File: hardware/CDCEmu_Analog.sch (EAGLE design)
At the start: 63 parts, among them J1 Audio In, J2 Audio Out, J3 Mic In, Q1 PCH, Q2 NCH, Q3 NCH, Q4 PCH, Q5 NCH, Q6 NPN, Q7 NPN, Q8 NPN, Q9 NPN, U1 1117, U2 BK8000L, U3 NE5532D

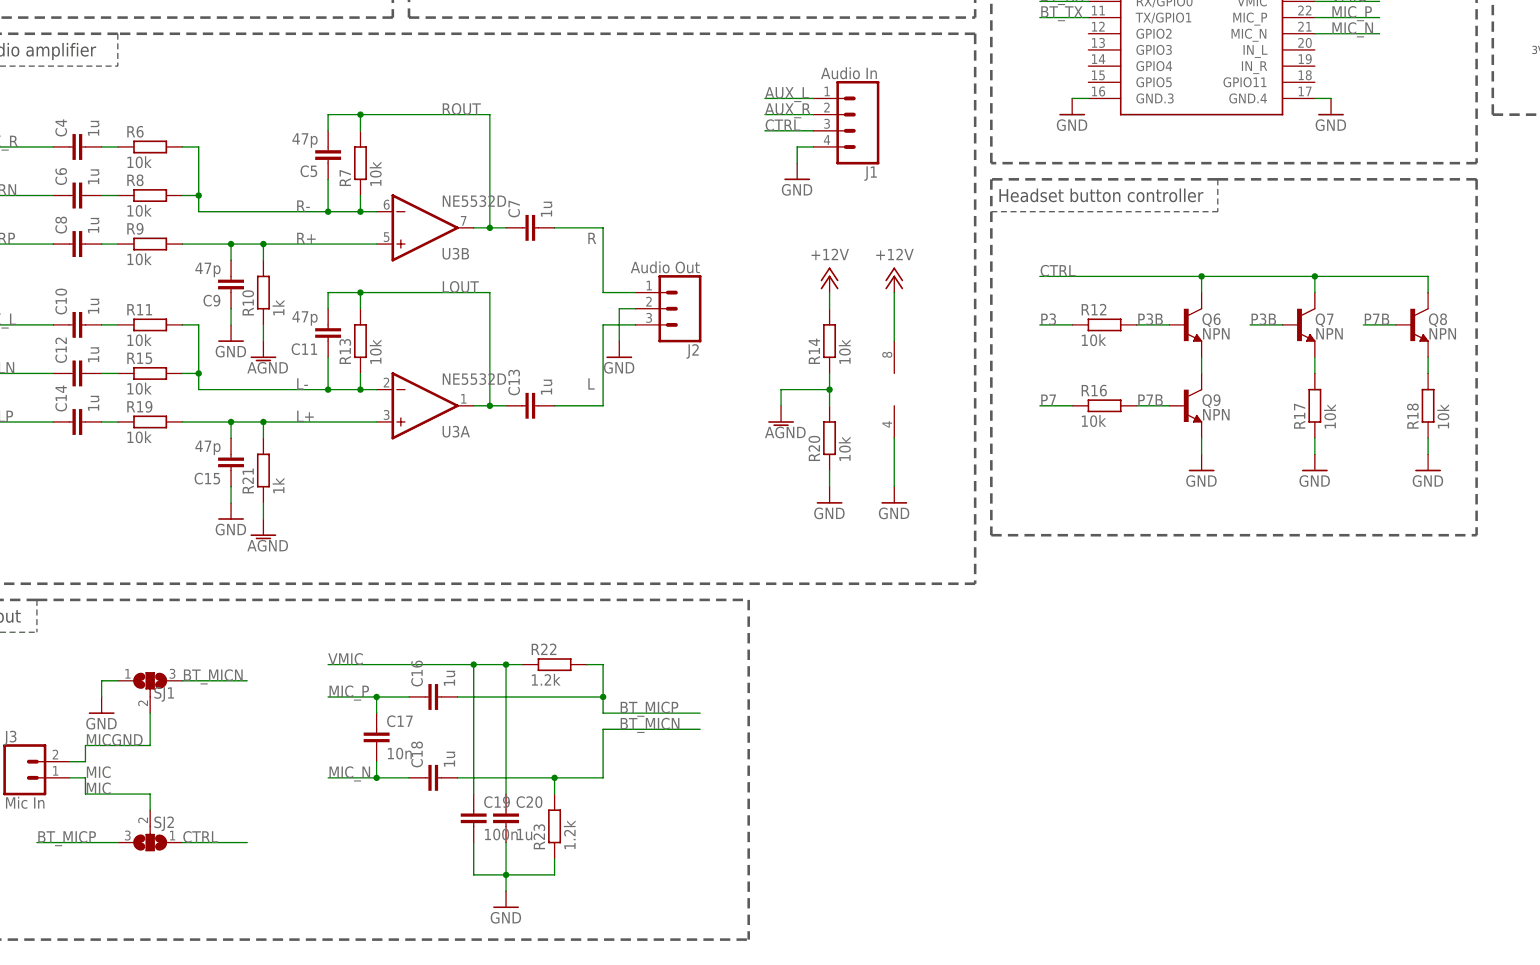
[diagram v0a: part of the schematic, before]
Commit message: [HW] Add audio gain control trimpots
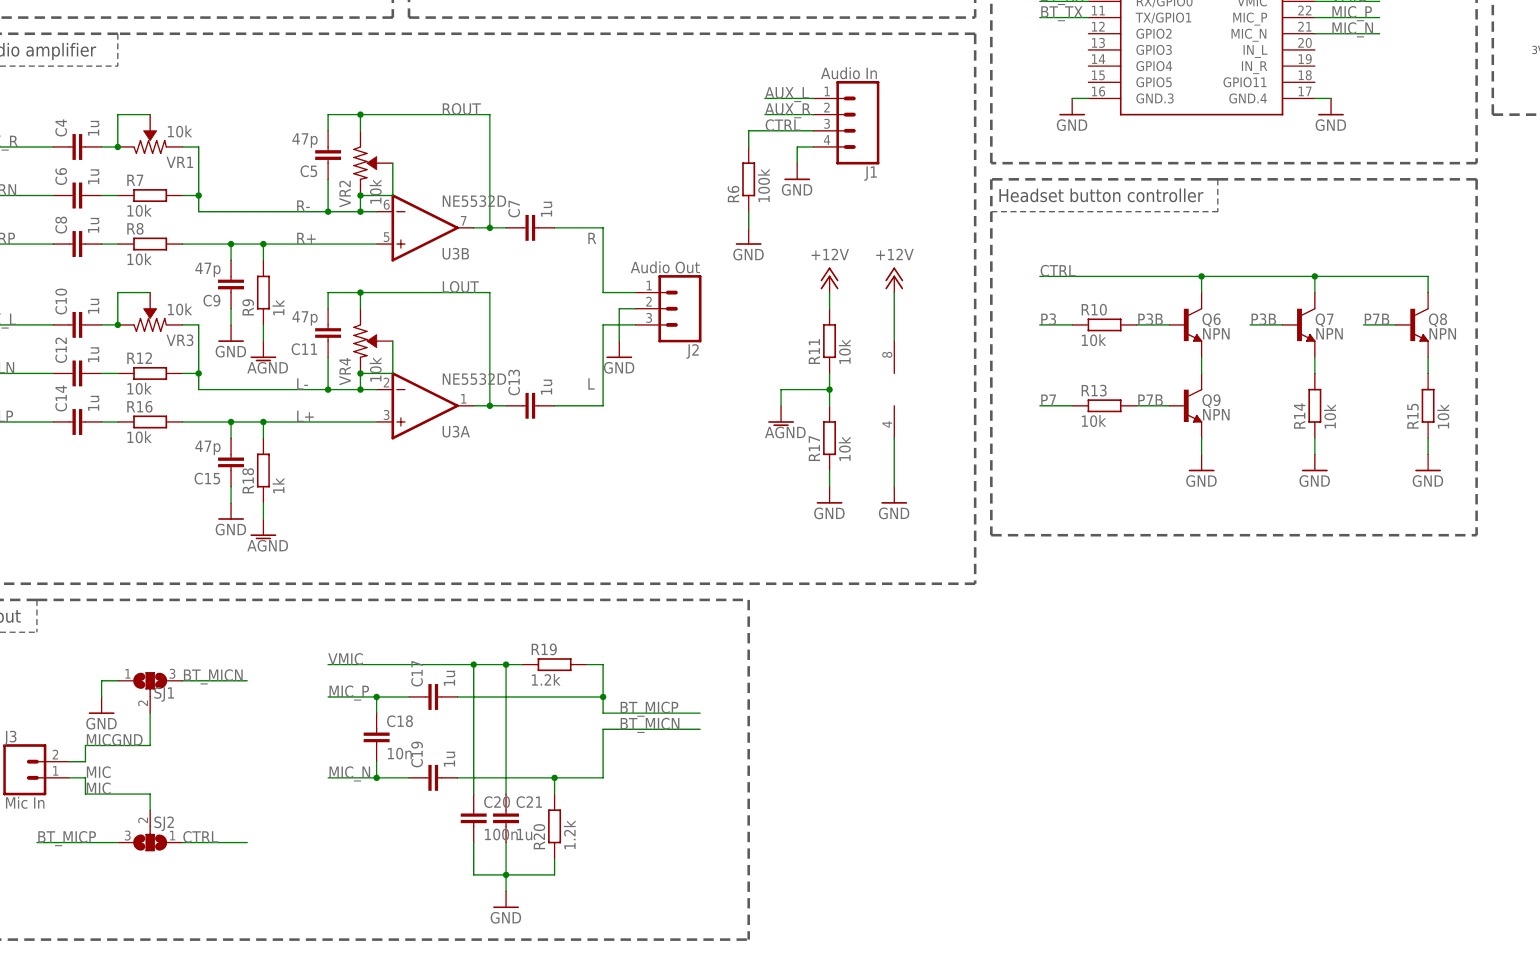
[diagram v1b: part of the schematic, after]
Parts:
- removed C16: 1u, rcl:C-EUC0805
- removed R21: 1k, rcl:R-EU_R0805
- removed R22, R23: 1.2k, rcl:R-EU_R0805
- added C21: 1u, rcl:C-EUC0805
- added VR1, VR2, VR3, VR4: 10k, SparkFun-Resistors:TRIMPOT-SMD-3MM-OPEN-1/10W-25%
- C17: value 10n -> 1u
- C18: value 1u -> 10n
- C19: value 100n -> 1u
- C20: value 1u -> 100n
- R10: value 1k -> 10k
- R18, R9: value 10k -> 1k
- R19, R20: value 10k -> 1.2k
- R6: value 10k -> 100k
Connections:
- net +12V: now also R11.2; no longer R14.2
- net AGND: now also R11.1, R17.2, R18.1, R9.1; no longer R10.1, R14.1, R20.2, R21.1
- net BT_MICN: now also C19.2, R20.2; no longer C18.2, R23.2
- net BT_MICP: now also C17.2, R19.2; no longer C16.2, R22.2
- net CTRL: now also R6.2
- net GND: now also C21.2, R14.1, R15.1, R6.1; no longer C19.2, R18.1, R23.1
- net L+: now also R16.2, R18.2; no longer R19.2, R21.2
- net L-: now also R12.2, VR3.CCW, VR4.CCW, VR4.WIPER; no longer R11.2, R13.1, R15.2
- net L1: now also VR3.CW, VR3.WIPER; no longer R11.1
- net L2: now also R12.1; no longer R15.1
- net L3: now also R16.1; no longer R19.1
- net LOUT: now also VR4.CW; no longer R13.2
- net MIC_N: now also C18.2, C19.1; no longer C17.2, C18.1
- net MIC_P: now also C18.1; no longer C16.1
- net P3: now also R10.1; no longer R12.1
- net P3B: now also R10.2; no longer R12.2
- net P7: now also R13.1; no longer R16.1
- net P7B: now also R13.2; no longer R16.2
- net Q7E: now also R14.2; no longer R17.2
- net Q8E: now also R15.2; no longer R18.2
- net R+: now also R8.2; no longer R10.2
- net R-: now also R7.2, VR1.CCW, VR2.CCW, VR2.WIPER; no longer R6.2, R7.1, R8.2
- net R1: now also VR1.CW, VR1.WIPER; no longer R6.1
- net R2: now also R7.1; no longer R8.1
- net R3: now also R8.1; no longer R9.1
- net ROUT: now also VR2.CW; no longer R7.2
- net VMIC: now also C21.1, R19.1; no longer C19.1, R22.1
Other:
- moved on the sheet: C17, C18, C19, C20, R10, R11, R12, R13, R14, R15, R16, R17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

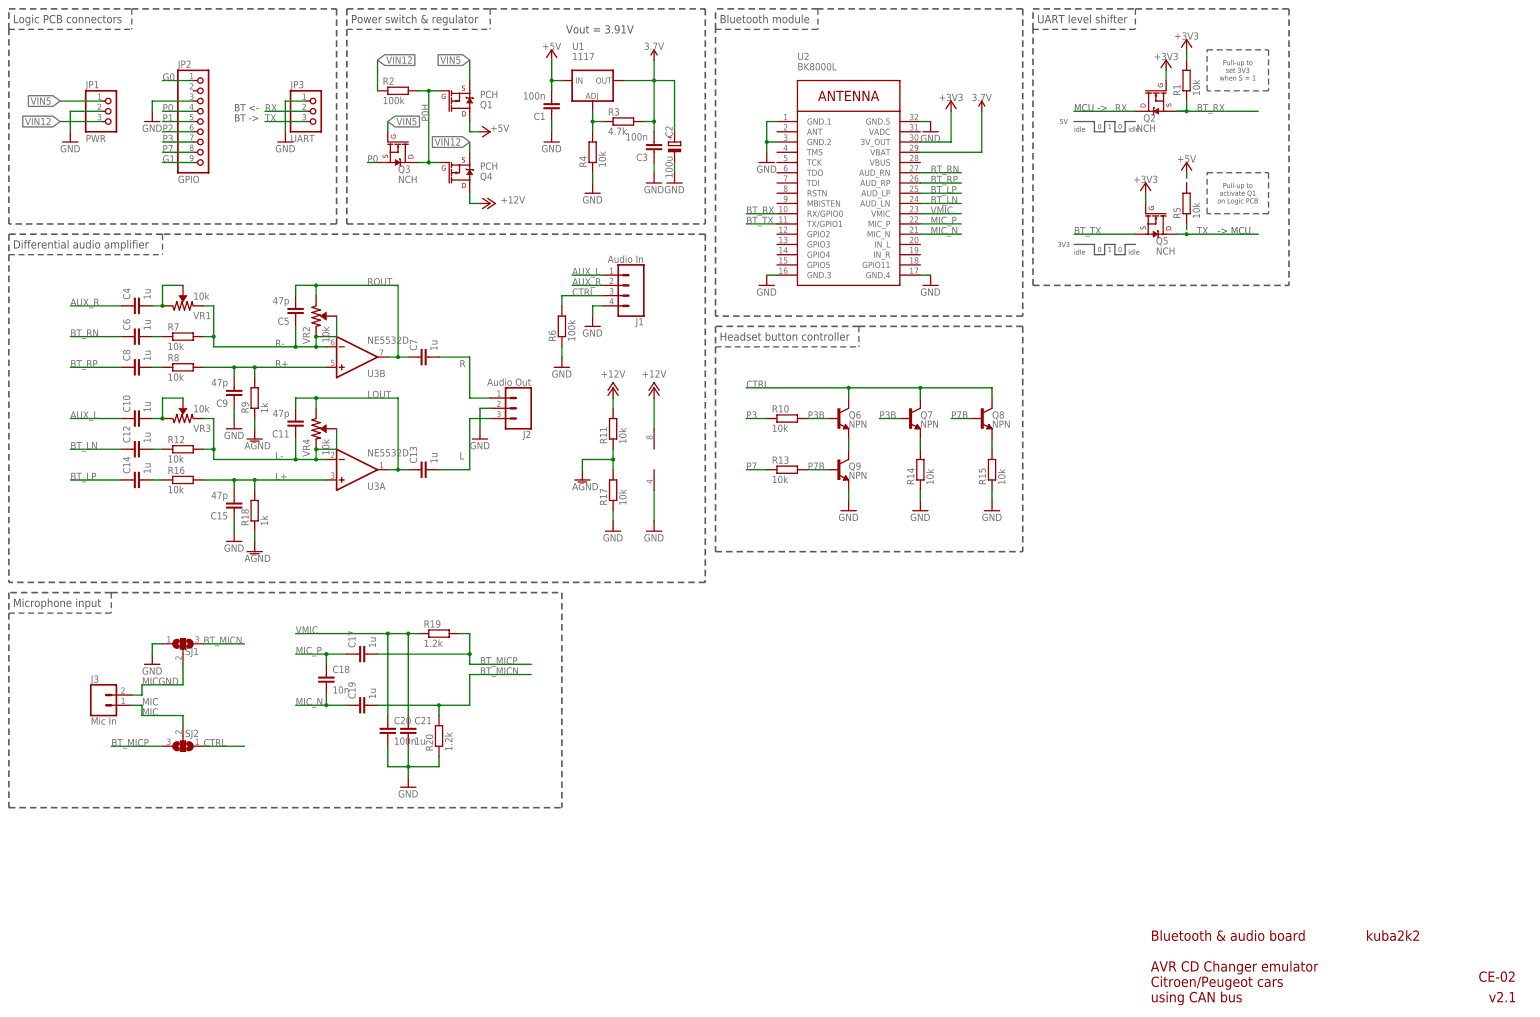
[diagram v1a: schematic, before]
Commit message: [HW/Analog] Add audio signal detection
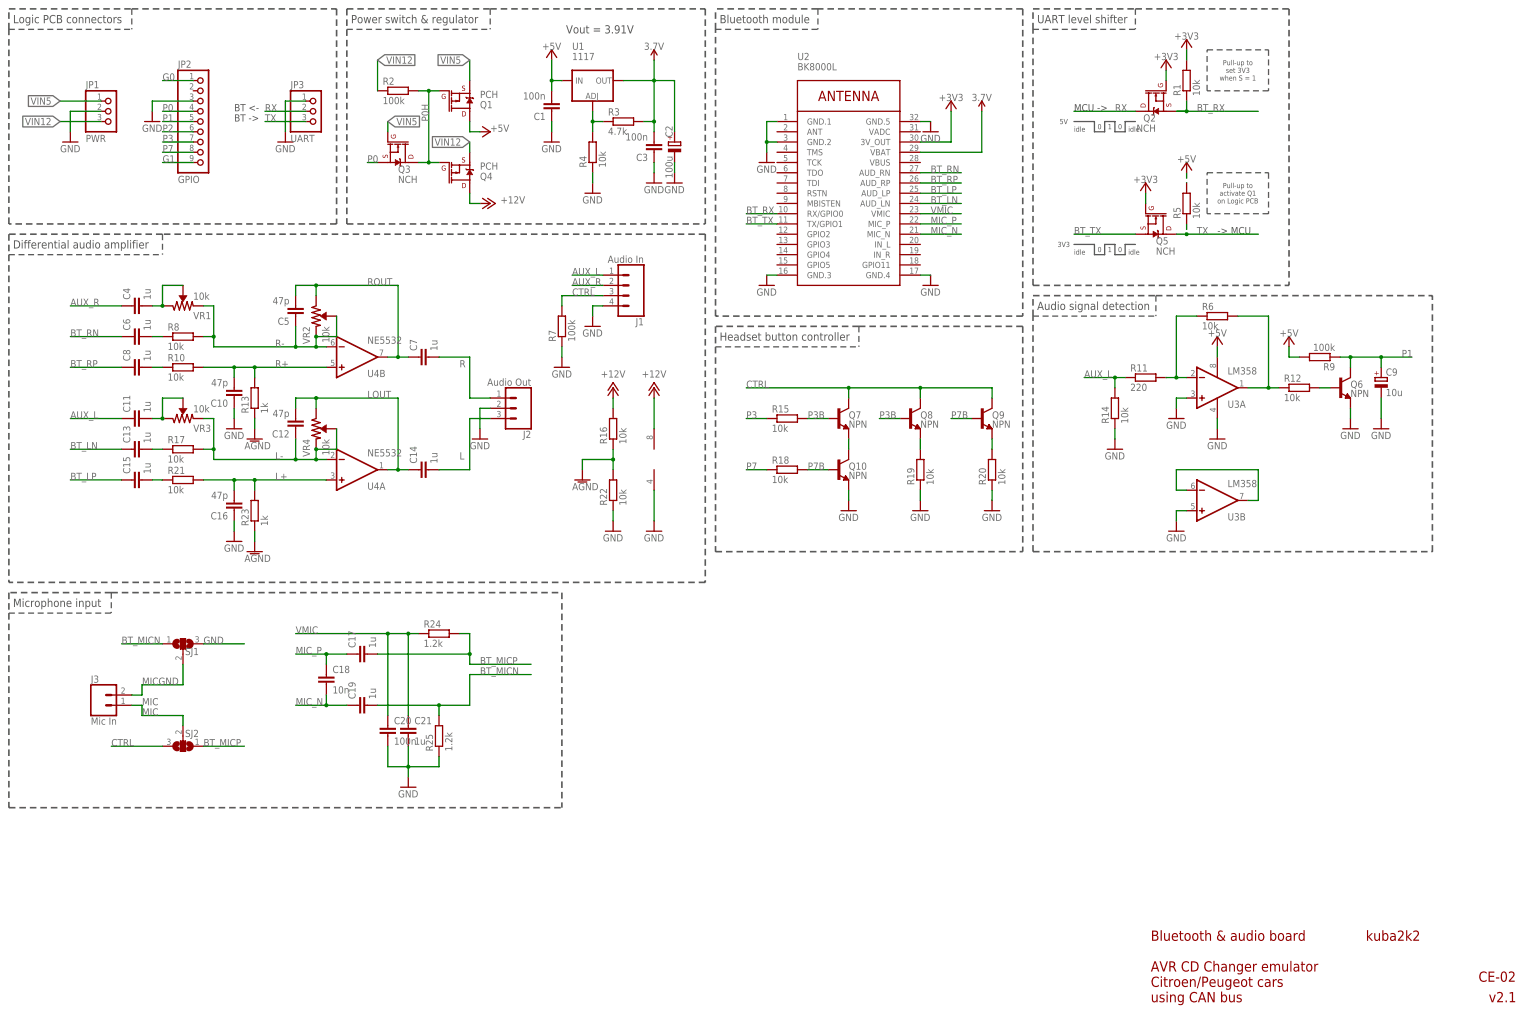
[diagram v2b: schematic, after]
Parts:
- added C16: 47p, rcl:C-EUC0805
- added Q10: NPN, SparkFun-DiscreteSemi:TRANS_NPN-MMBTA42
- added R21, R22: 10k, rcl:R-EU_R0805
- added R23: 1k, rcl:R-EU_R0805
- added R24, R25: 1.2k, rcl:R-EU_R0805
- added U4: NE5532, custom:LM358D
- C10, C12: value 1u -> 47p
- C11, C15: value 47p -> 1u
- C9: value 47p -> 10u; device rcl:C-EUC0805 -> custom:CPOL-EUC1206
- R11: value 10k -> 220
- R13: value 10k -> 1k
- R18: value 1k -> 10k
- R19, R20: value 1.2k -> 10k
- R6: value 100k -> 10k
- R7: value 10k -> 100k
- R9: value 1k -> 100k
- U3: value NE5532D -> LM358; device linear:NE5532D -> custom:LM358D
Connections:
- new net DET-: R11.2, R6.1, U3A.-IN
- new net DETOUT: R12.1, R6.2, U3A.OUT
- new net DET_B: Q6.B, R12.2
- new net U4FB: U3B.-IN, U3B.OUT
- net +12V: now also R16.2, U4P.V+; no longer R11.2, U3P.V+
- net +5V: now also R9.2, U3P.V+
- net AGND: now also R13.1, R16.1, R22.2, R23.1; no longer R11.1, R17.2, R18.1, R9.1
- net AUX_L: now also C11.1, R11.1, R14.2; no longer C10.1
- net BT_LN: now also C13.1; no longer C12.1
- net BT_LP: now also C15.1; no longer C14.1
- net BT_MICN: now also R25.2, SJ1.1; no longer R20.2, SJ1.3
- net BT_MICP: now also R24.2, SJ2.1; no longer R19.2, SJ2.3
- net CCE: now also Q10.C, Q7.E; no longer Q6.E, Q9.C
- net CTRL: now also Q9.C, R7.2, SJ2.3; no longer Q6.C, R6.2, SJ2.1
- net GND: now also C10.1, C16.1, C9.-, Q10.E, Q6.E, R19.1, R22.1, R25.1, R7.1, SJ1.3, U3A.+IN, U3B.+IN, U4P.V-; no longer C15.1, C9.1, Q9.E, R15.1, R17.1, R6.1, SJ1.1
- net L: now also C14.2; no longer C13.2
- net L+: now also C16.2, R21.2, R23.2, U4A.+IN; no longer C15.2, R16.2, R18.2, U3A.+IN
- net L-: now also C12.1, R17.2, U4A.-IN; no longer C11.1, R12.2, U3A.-IN
- net L1: now also C11.2; no longer C10.2
- net L2: now also C13.2, R17.1; no longer C12.2, R12.1
- net L3: now also C15.2, R21.1; no longer C14.2, R16.1
- net LOUT: now also C12.2, C14.1, U4A.OUT; no longer C11.2, C13.1, U3A.OUT
- net P1: now also C9.+, Q6.C, R9.1
- net P3: now also R15.1; no longer R10.1
- net P3B: now also Q8.B, R15.2; no longer Q6.B, R10.2
- net P7: now also R18.1; no longer R13.1
- net P7B: now also Q10.B, R18.2; no longer Q8.B, R13.2
- net Q7E: now also Q8.E, R19.2; no longer Q7.E, R14.2
- net Q8E: now also Q9.E, R20.2; no longer Q8.E, R15.2
- net R+: now also C10.2, R10.2, R13.2, U4B.+IN; no longer C9.2, R8.2, R9.2, U3B.+IN
- net R-: now also R8.2, U4B.-IN; no longer R7.2, U3B.-IN
- net R2: now also R8.1; no longer R7.1
- net R3: now also R10.1; no longer R8.1
- net ROUT: now also U4B.OUT; no longer U3B.OUT
- net VMIC: now also R24.1; no longer R19.1
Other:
- note added: "Audio signal detection"
- moved on the sheet: C10, C11, C12, C13, C14, C15, Q6, Q7, Q8, Q9, R10, R11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

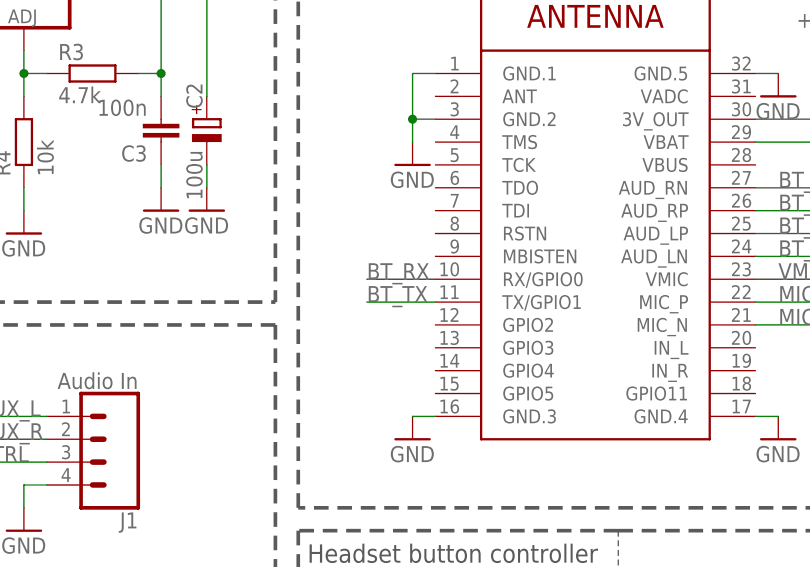
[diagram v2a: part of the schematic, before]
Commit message: [HW/Analog] Fix swapped Bluetooth RX and TX
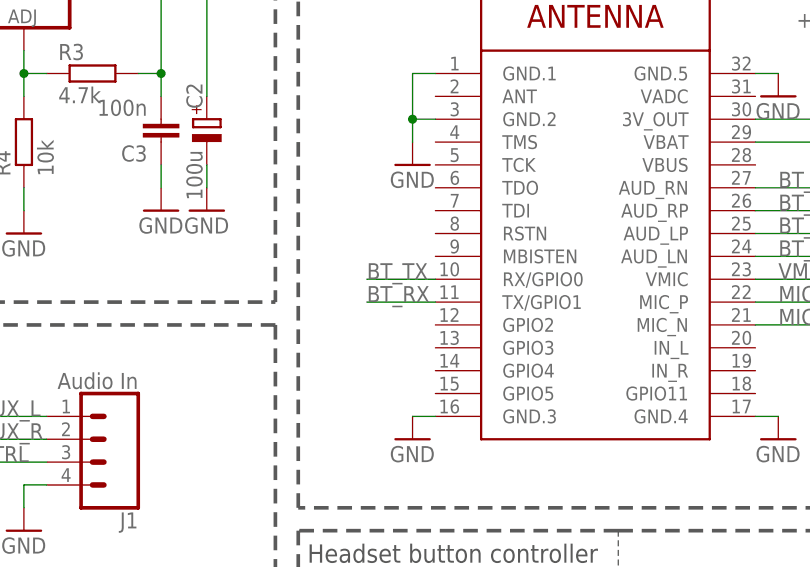
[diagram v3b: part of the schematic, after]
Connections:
- net BT_RX: now also U2.TX/GPIO1; no longer U2.RX/GPIO0
- net BT_TX: now also U2.RX/GPIO0; no longer U2.TX/GPIO1
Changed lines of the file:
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@@
 </segment>
 <segment>
-<pinref part="U2" gate="G$1" pin="RX/GPIO0"/>
-<wire x1="190.5" y1="73.66" x2="182.88" y2="73.66" width="0.1524" layer="91"/>
-<label x="182.88" y="73.66" size="1.778" layer="95"/>
+<pinref part="U2" gate="G$1" pin="TX/GPIO1"/>
+<wire x1="190.5" y1="71.12" x2="182.88" y2="71.12" width="0.1524" layer="91"/>
+<label x="182.88" y="71.12" size="1.778" layer="95"/>
 </segment>
 </net>
@@
 </segment>
 <segment>
-<pinref part="U2" gate="G$1" pin="TX/GPIO1"/>
-<wire x1="190.5" y1="71.12" x2="182.88" y2="71.12" width="0.1524" layer="91"/>
-<label x="182.88" y="71.12" size="1.778" layer="95"/>
+<pinref part="U2" gate="G$1" pin="RX/GPIO0"/>
+<wire x1="190.5" y1="73.66" x2="182.88" y2="73.66" width="0.1524" layer="91"/>
+<label x="182.88" y="73.66" size="1.778" layer="95"/>
 </segment>
 </net>
